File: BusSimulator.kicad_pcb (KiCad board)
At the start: 2 copper layers, 101.6 x 53.3 mm, 18 parts, among them J1 CONN_3-6318491-6, J2 CONN_3-6318491-6, U1 MPM3620, U2 MPM3620

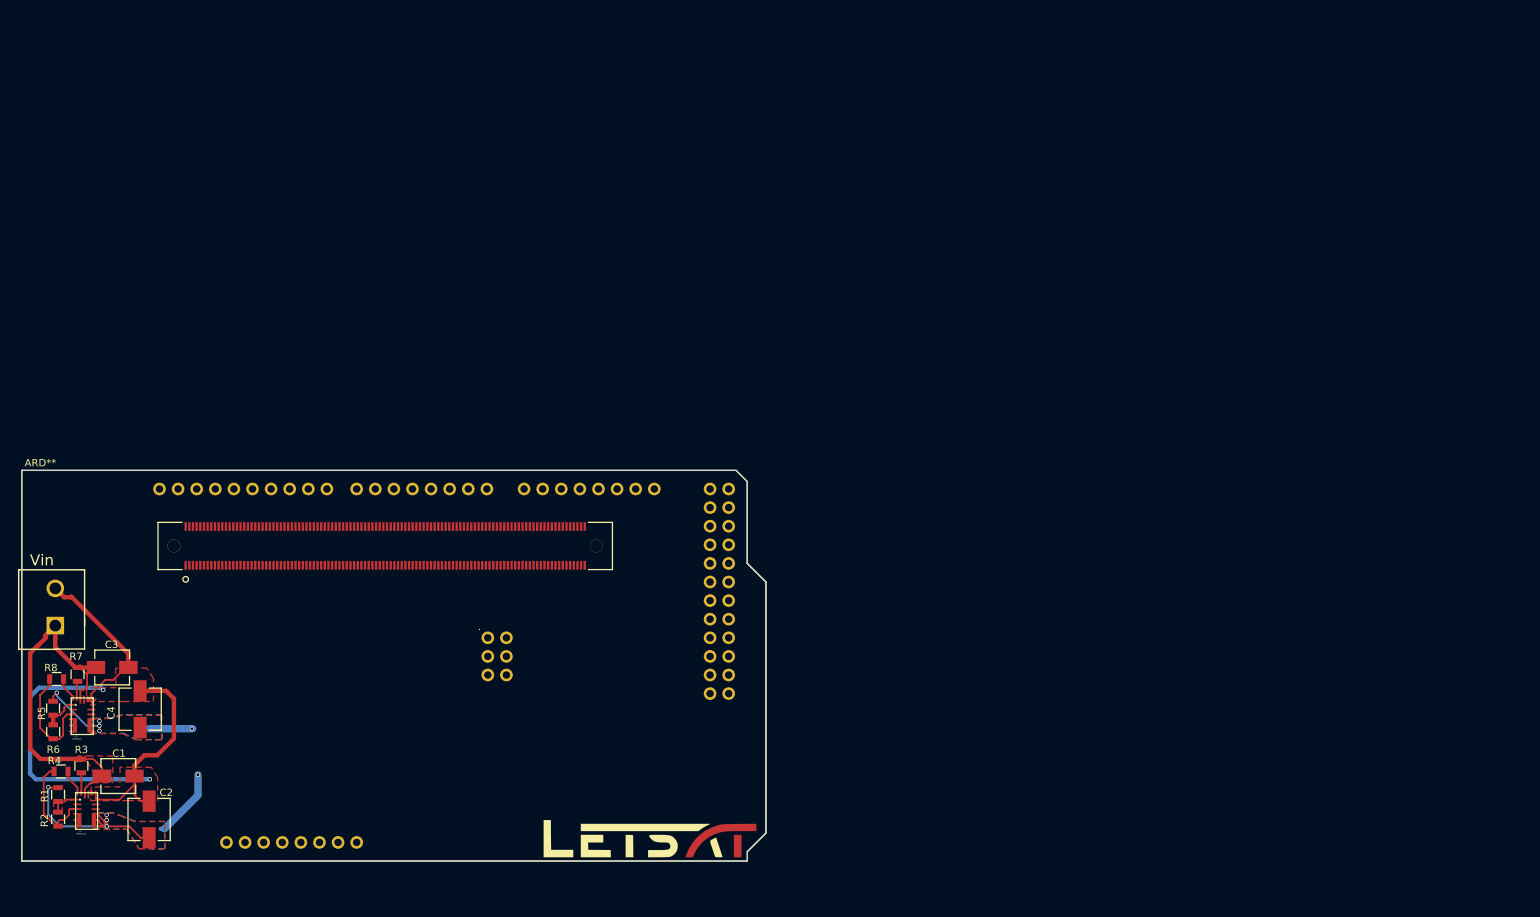
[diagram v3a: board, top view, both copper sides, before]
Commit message: pushed components on the pcb
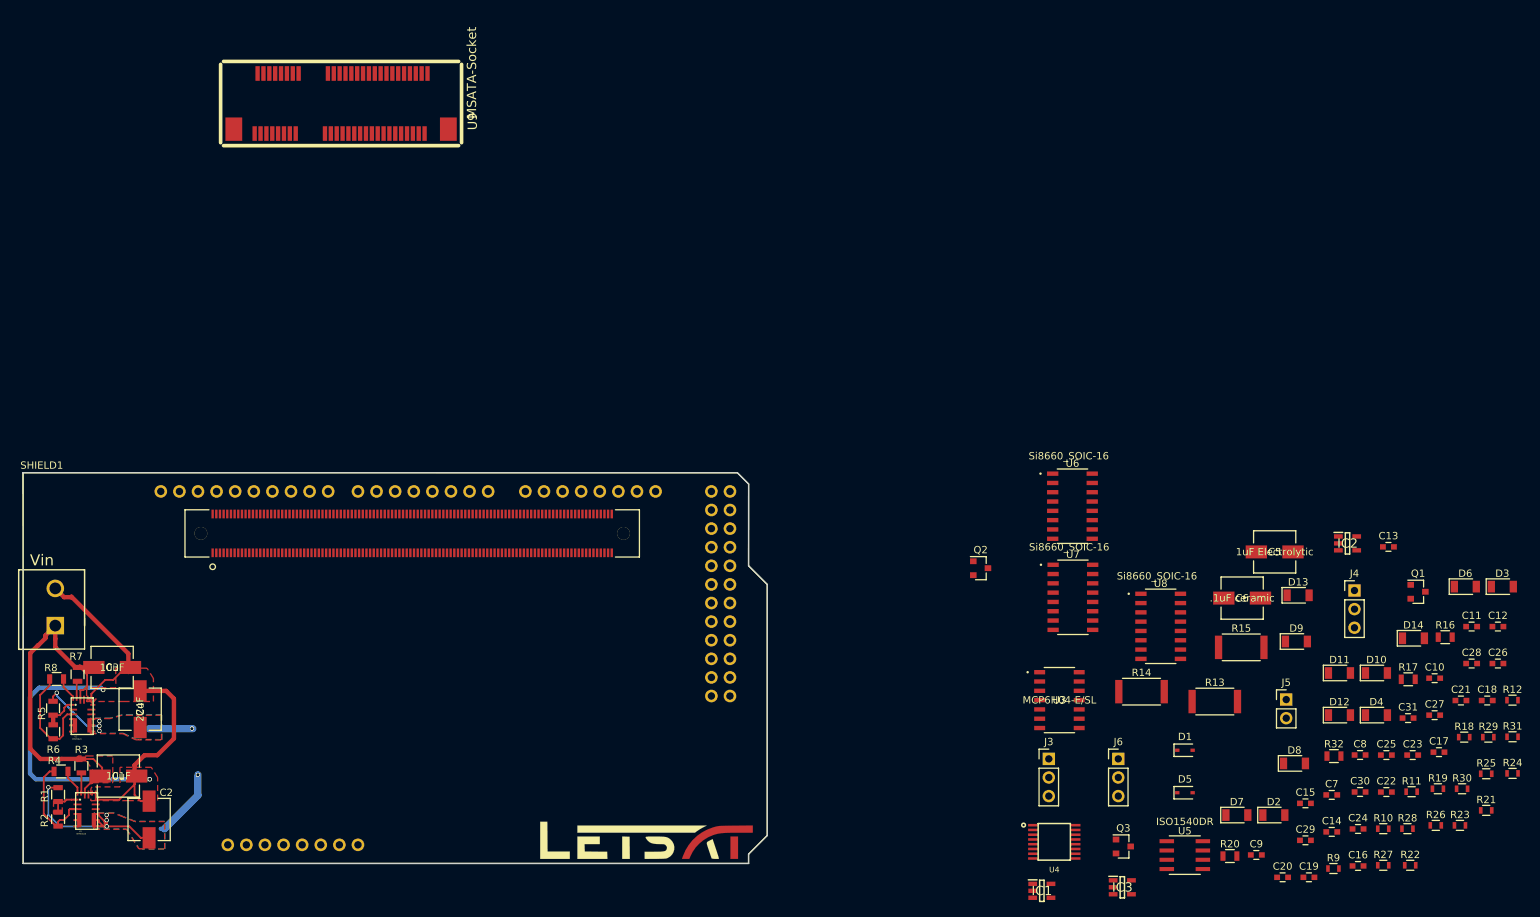
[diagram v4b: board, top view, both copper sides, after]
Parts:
- removed ARD**: Arduino_Due_Shield, BusSimulator:Arduino_Due_Shield
- added C10: .1uF, Capacitors_SMD:C_0603, F.Cu at (302.9, 116.6)
- added C11: .1uF, Capacitors_SMD:C_0603, F.Cu at (308.0, 109.6)
- added C12: .1uF, Capacitors_SMD:C_0603, F.Cu at (311.6, 109.6)
- added C13: .1uF, Capacitors_SMD:C_0603, F.Cu at (296.6, 98.7)
- added C14: .1uF, Capacitors_SMD:C_0603, F.Cu at (288.9, 137.6)
- added C15: .1uF, Capacitors_SMD:C_0603, F.Cu at (285.3, 133.7)
- added C16: .1uF, Capacitors_SMD:C_0603, F.Cu at (292.5, 142.3)
- added C17: .1uF, Capacitors_SMD:C_0603, F.Cu at (303.5, 126.7)
- added C18: .1uF, Capacitors_SMD:C_0603, F.Cu at (310.1, 119.7)
- added C19: .1uF, Capacitors_SMD:C_0603, F.Cu at (285.8, 143.8)
- added C20: .1uF, Capacitors_SMD:C_0603, F.Cu at (282.2, 143.8)
- added C21: .1uF, Capacitors_SMD:C_0603, F.Cu at (306.5, 119.7)
- added C22: .1uF, Capacitors_SMD:C_0603, F.Cu at (296.3, 132.2)
- added C23: .1uF, Capacitors_SMD:C_0603, F.Cu at (299.9, 127.1)
- added C24: .1uF, Capacitors_SMD:C_0603, F.Cu at (292.5, 137.2)
- added C25: .1uF, Capacitors_SMD:C_0603, F.Cu at (296.3, 127.1)
- added C26: .1uF, Capacitors_SMD:C_0603, F.Cu at (311.6, 114.6)
- added C27: .1uF, Capacitors_SMD:C_0603, F.Cu at (302.9, 121.7)
- added C28: .1uF, Capacitors_SMD:C_0603, F.Cu at (308.0, 114.6)
- added C29: .1uF, Capacitors_SMD:C_0603, F.Cu at (285.3, 138.8)
- added C30: .1uF, Capacitors_SMD:C_0603, F.Cu at (292.7, 132.2)
- added C31: .1uF, Capacitors_SMD:C_0603, F.Cu at (299.3, 122.1)
- added C5: 1uF Electrolytic, BusSimulator:C22, F.Cu at (281.1, 99.4)
- added C6: .1uF ceramic, BusSimulator:C22, F.Cu at (276.6, 105.7)
- added C7: .1uF, Capacitors_SMD:C_0603, F.Cu at (288.9, 132.6)
- added C8: .1uF, Capacitors_SMD:C_0603, F.Cu at (292.7, 127.1)
- added C9: .1uF, Capacitors_SMD:C_0603, F.Cu at (278.6, 140.8)
- added D1: D_Zener 9V, Diodes_SMD:D_SOD-323, F.Cu at (268.8, 126.5)
- added D10: LED, Diodes_SMD:D_1206, F.Cu at (295.0, 115.9)
- added D11: LED, Diodes_SMD:D_1206, F.Cu at (289.9, 115.9)
- added D12: LED, Diodes_SMD:D_1206, F.Cu at (289.9, 121.7)
- added D13: LED, Diodes_SMD:D_1206, F.Cu at (284.3, 105.3)
- added D14: LED, Diodes_SMD:D_1206, F.Cu at (300.0, 111.2)
- added D2: LED, Diodes_SMD:D_1206, F.Cu at (281.0, 135.3)
- added D3: LED, Diodes_SMD:D_1206, F.Cu at (312.2, 104.1)
- added D4: LED, Diodes_SMD:D_1206, F.Cu at (295.0, 121.7)
- added D5: D_Zener 9V, Diodes_SMD:D_SOD-323, F.Cu at (268.8, 132.3)
- added D6: LED, Diodes_SMD:D_1206, F.Cu at (307.1, 104.1)
- added D7: LED, Diodes_SMD:D_1206, F.Cu at (275.9, 135.3)
- added D8: LED, Diodes_SMD:D_1206, F.Cu at (283.8, 128.3)
- added D9: LED, Diodes_SMD:D_1206, F.Cu at (284.0, 111.6)
- added IC1: CS30CL, BusSimulator:SOT95P280X145-5N, F.Cu at (249.3, 145.7)
- added IC2: CS30CL, BusSimulator:SOT95P280X145-5N, F.Cu at (291.0, 98.2)
- added IC3: CS30CL, BusSimulator:SOT95P280X145-5N, F.Cu at (260.3, 145.2)
- added J3: Conn_01x03, Pin_Headers:Pin_Header_Straight_1x03_Pitch2.54mm, F.Cu at (250.2, 127.6)
- added J4: Conn_01x03, Pin_Headers:Pin_Header_Straight_1x03_Pitch2.54mm, F.Cu at (292.0, 104.7)
- added J5: Conn_01x02, Pin_Headers:Pin_Header_Straight_1x02_Pitch2.54mm, F.Cu at (282.7, 119.5)
- added J6: Conn_01x03, Pin_Headers:Pin_Header_Straight_1x03_Pitch2.54mm, F.Cu at (259.7, 127.6)
- added Q1: MOSFET_N, TO_SOT_Packages_SMD:SOT-23, F.Cu at (300.7, 104.8)
- added Q2: MOSFET_N, TO_SOT_Packages_SMD:SOT-23, F.Cu at (240.9, 101.6)
- added Q3: MOSFET_N, TO_SOT_Packages_SMD:SOT-23, F.Cu at (260.4, 139.6)
- added R10: 10k, Resistors_SMD:R_0603, F.Cu at (295.9, 137.2)
- added R11: 30k, Resistors_SMD:R_0603, F.Cu at (299.8, 132.1)
- added R12: 10k, Resistors_SMD:R_0603, F.Cu at (313.6, 119.6)
- added R13: Dummy Load, Resistors_SMD:R_2512, F.Cu at (272.9, 119.8)
- added R14: Dummy Load, Resistors_SMD:R_2512, F.Cu at (262.9, 118.5)
- added R15: Dummy Load, Resistors_SMD:R_2512, F.Cu at (276.5, 112.4)
- added R16: 25m, Resistors_SMD:R_0805, F.Cu at (304.4, 111.0)
- added R17: 25m, Resistors_SMD:R_0805, F.Cu at (299.3, 116.8)
- added R18: 1k, Resistors_SMD:R_0603, F.Cu at (307.0, 124.7)
- added R19: 330, Resistors_SMD:R_0603, F.Cu at (303.4, 131.7)
- added R20: 25m, Resistors_SMD:R_0805, F.Cu at (275.0, 140.9)
- added R21: 180, Resistors_SMD:R_0603, F.Cu at (310.0, 134.7)
- added R22: 100k, Resistors_SMD:R_0603, F.Cu at (299.6, 142.2)
- added R23: 330, Resistors_SMD:R_0603, F.Cu at (306.4, 136.7)
- added R24: 180, Resistors_SMD:R_0603, F.Cu at (313.6, 129.6)
- added R25: 1k, Resistors_SMD:R_0603, F.Cu at (310.0, 129.7)
- added R26: 330, Resistors_SMD:R_0603, F.Cu at (303.1, 136.7)
- added R27: 330, Resistors_SMD:R_0603, F.Cu at (295.9, 142.2)
- added R28: 330, Resistors_SMD:R_0603, F.Cu at (299.2, 137.2)
- added R29: 330, Resistors_SMD:R_0603, F.Cu at (310.3, 124.7)
- added R30: 330, Resistors_SMD:R_0603, F.Cu at (306.7, 131.7)
- added R31: 330, Resistors_SMD:R_0603, F.Cu at (313.6, 124.6)
- added R32: 0, Resistors_SMD:R_0805, F.Cu at (289.2, 127.3)
- added R9: 10k, Resistors_SMD:R_0603, F.Cu at (289.1, 142.6)
- added SHIELD1: ARDUINO_DUE_SHIELD, BusSimulator:Arduino_Due_Shield, F.Cu at (110.2, 141.9)
- added U3: MCP6H04-E/SL, BusSimulator:MCP6H04-E, F.Cu at (251.7, 119.6)
- added U4: ADC128D818CIMTX, BusSimulator:ADC128D818CIMTX, F.Cu at (251.0, 139.0)
- added U5: ISO1540DR, BusSimulator:ISO1540DR, F.Cu at (268.8, 140.8)
- added U6: Si8660_SOIC-16, BusSimulator:SI8660BA-B-IS1, F.Cu at (253.5, 93.1)
- added U7: Si8660_SOIC-16, BusSimulator:SI8660BA-B-IS1, F.Cu at (253.5, 105.6)
- added U8: Si8660_SOIC-16, BusSimulator:SI8660BA-B-IS1, F.Cu at (265.5, 109.5)
- added U9: MSATA-Socket, BusSimulator:msata-socket, F.Cu at (141.1, 38.2)
- C1, C3: footprint BusSimulator:EEE-1EA100WR -> BusSimulator:C22
- C4: footprint BusSimulator:EEE-1EA220WR -> BusSimulator:C22
- J2: value CONN_3-6318491-6 -> OSTTA024163
- moved J1 4.06 mm to (128.6, 94.2)
- moved G1 0.53 mm to (195.4, 139.0)
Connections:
- net +12V renamed 12v_sense
- net +3V3 renamed +3.3V
- C1 pad 1: GNDREF -> mCOM_GND
- C2 pad 1: GNDREF -> mCOM_GND
- C2 pad 2: +5V -> mCOM_5V_SBY
- C3 pad 1: GNDREF -> mCOM_GND
- C4 pad 1: GNDREF -> mCOM_GND
- J1 pad 1: (no net) -> mCOM_GND
- J1 pad 10: (no net) -> Net-(J1-Pad10)
- J1 pad 100: (no net) -> mCOM_GND
- J1 pad 101: (no net) -> Net-(J1-Pad101)
- J1 pad 102: (no net) -> Net-(J1-Pad102)
- J1 pad 103: (no net) -> Net-(J1-Pad103)
- J1 pad 104: (no net) -> mCOM_12V
- J1 pad 105: (no net) -> mCOM_12V
- J1 pad 106: (no net) -> mCOM_12V
- J1 pad 107: (no net) -> mCOM_12V
- J1 pad 108: (no net) -> mCOM_12V
- J1 pad 109: (no net) -> mCOM_12V
- J1 pad 11: (no net) -> mCOM_GND
- J1 pad 110: (no net) -> mCOM_GND
- J1 pad 111: (no net) -> mCOM_GND
- J1 pad 112: (no net) -> Net-(J1-Pad112)
- J1 pad 113: (no net) -> Net-(J1-Pad113)
- J1 pad 114: (no net) -> Net-(J1-Pad114)
- J1 pad 115: (no net) -> Net-(J1-Pad115)
- J1 pad 116: (no net) -> Net-(J1-Pad116)
- J1 pad 117: (no net) -> Net-(J1-Pad117)
- J1 pad 118: (no net) -> Net-(J1-Pad118)
- J1 pad 119: (no net) -> Net-(J1-Pad119)
- J1 pad 12: (no net) -> Net-(J1-Pad12)
- J1 pad 120: (no net) -> Net-(J1-Pad120)
- J1 pad 121: (no net) -> mCOM_GND
- J1 pad 122: (no net) -> PWRBTNn
- J1 pad 123: (no net) -> Net-(J1-Pad123)
- J1 pad 124: (no net) -> Net-(J1-Pad124)
- J1 pad 125: (no net) -> Net-(J1-Pad125)
- J1 pad 126: (no net) -> Net-(J1-Pad126)
- J1 pad 127: (no net) -> Net-(J1-Pad127)
- J1 pad 128: (no net) -> Net-(J1-Pad128)
- J1 pad 129: (no net) -> Net-(J1-Pad129)
- J1 pad 13: (no net) -> Net-(J1-Pad13)
- J1 pad 130: (no net) -> Net-(J1-Pad130)
- J1 pad 131: (no net) -> mCOM_GND
- J1 pad 132: (no net) -> Net-(J1-Pad132)
- J1 pad 133: (no net) -> Net-(J1-Pad133)
- J1 pad 134: (no net) -> PWR_OK
- J1 pad 135: (no net) -> Net-(J1-Pad135)
- J1 pad 136: (no net) -> Net-(J1-Pad136)
- J1 pad 137: (no net) -> Net-(J1-Pad137)
- J1 pad 138: (no net) -> Net-(J1-Pad138)
- J1 pad 139: (no net) -> Net-(J1-Pad139)
- J1 pad 14: (no net) -> Net-(J1-Pad14)
- J1 pad 140: (no net) -> Net-(J1-Pad140)
- J1 pad 141: (no net) -> mCOM_GND
- J1 pad 142: (no net) -> Net-(J1-Pad142)
- J1 pad 143: (no net) -> I2C_CK
- J1 pad 144: (no net) -> I2C_DAT
- J1 pad 145: (no net) -> Net-(J1-Pad145)
- J1 pad 146: (no net) -> Net-(J1-Pad146)
- J1 pad 147: (no net) -> Net-(J1-Pad147)
- J1 pad 148: (no net) -> Net-(J1-Pad148)
- J1 pad 149: (no net) -> Net-(J1-Pad149)
- J1 pad 15: (no net) -> Net-(J1-Pad15)
- J1 pad 150: (no net) -> Net-(J1-Pad150)
- J1 pad 151: (no net) -> mCOM_GND
- J1 pad 152: (no net) -> Net-(J1-Pad152)
- J1 pad 153: (no net) -> Net-(J1-Pad153)
- J1 pad 154: (no net) -> Net-(J1-Pad154)
- J1 pad 155: (no net) -> Net-(J1-Pad155)
- J1 pad 156: (no net) -> Net-(J1-Pad156)
- J1 pad 157: (no net) -> Net-(J1-Pad157)
- J1 pad 158: (no net) -> Net-(J1-Pad158)
- J1 pad 159: (no net) -> SYS_RESETn
- J1 pad 16: (no net) -> SATA0_TX+
- J1 pad 160: (no net) -> Net-(J1-Pad160)
- J1 pad 161: (no net) -> mCOM_GND
- J1 pad 162: (no net) -> Net-(J1-Pad162)
- J1 pad 163: (no net) -> Net-(J1-Pad163)
- J1 pad 164: (no net) -> GPO1
- J1 pad 165: (no net) -> Net-(J1-Pad165)
- J1 pad 166: (no net) -> Net-(J1-Pad166)
- J1 pad 167: (no net) -> GPO2
- J1 pad 168: (no net) -> Net-(J1-Pad168)
- J1 pad 169: (no net) -> Net-(J1-Pad169)
- J1 pad 17: (no net) -> SATA0_TX-
- J1 pad 170: (no net) -> mCOM_GND
- J1 pad 171: (no net) -> Net-(J1-Pad171)
- J1 pad 172: (no net) -> Net-(J1-Pad172)
- J1 pad 173: (no net) -> GPO3
- J1 pad 174: (no net) -> Net-(J1-Pad174)
- J1 pad 175: (no net) -> Net-(J1-Pad175)
- J1 pad 176: (no net) -> Net-(J1-Pad176)
- J1 pad 177: (no net) -> WAKE1n
- J1 pad 178: (no net) -> Net-(J1-Pad178)
- J1 pad 179: (no net) -> Net-(J1-Pad179)
- J1 pad 18: (no net) -> Net-(J1-Pad18)
- J1 pad 180: (no net) -> mCOM_GND
- J1 pad 181: (no net) -> Net-(J1-Pad181)
- J1 pad 182: (no net) -> Net-(J1-Pad182)
- J1 pad 183: (no net) -> Net-(J1-Pad183)
- J1 pad 184: (no net) -> Net-(J1-Pad184)
- J1 pad 185: (no net) -> Net-(J1-Pad185)
- J1 pad 186: (no net) -> Net-(J1-Pad186)
- J1 pad 187: (no net) -> Net-(J1-Pad187)
- J1 pad 188: (no net) -> Net-(J1-Pad188)
- J1 pad 189: (no net) -> Net-(J1-Pad189)
- J1 pad 19: (no net) -> SATA0_RX+
- J1 pad 190: (no net) -> mCOM_GND
- J1 pad 191: (no net) -> Net-(J1-Pad191)
- J1 pad 192: (no net) -> Net-(J1-Pad192)
- J1 pad 193: (no net) -> Net-(J1-Pad193)
- J1 pad 194: (no net) -> mCOM_5V_SBY
- J1 pad 195: (no net) -> mCOM_5V_SBY
- J1 pad 196: (no net) -> mCOM_5V_SBY
- J1 pad 197: (no net) -> mCOM_5V_SBY
- J1 pad 198: (no net) -> Net-(J1-Pad198)
- J1 pad 199: (no net) -> Net-(J1-Pad199)
- J1 pad 2: (no net) -> Net-(J1-Pad2)
- J1 pad 20: (no net) -> SATA0_RX-
- J1 pad 200: (no net) -> mCOM_GND
- J1 pad 201: (no net) -> Net-(J1-Pad201)
- J1 pad 202: (no net) -> Net-(J1-Pad202)
- J1 pad 203: (no net) -> Net-(J1-Pad203)
- J1 pad 204: (no net) -> Net-(J1-Pad204)
- J1 pad 205: (no net) -> Net-(J1-Pad205)
- J1 pad 206: (no net) -> Net-(J1-Pad206)
- J1 pad 207: (no net) -> Net-(J1-Pad207)
- J1 pad 208: (no net) -> Net-(J1-Pad208)
- J1 pad 209: (no net) -> Net-(J1-Pad209)
- J1 pad 21: (no net) -> mCOM_GND
- J1 pad 210: (no net) -> mCOM_GND
- J1 pad 211: (no net) -> Net-(J1-Pad211)
- J1 pad 212: (no net) -> Net-(J1-Pad212)
- J1 pad 213: (no net) -> SLEEPn
- J1 pad 214: (no net) -> mCOM_12V
- J1 pad 215: (no net) -> mCOM_12V
- J1 pad 216: (no net) -> mCOM_12V
- J1 pad 217: (no net) -> mCOM_12V
- J1 pad 218: (no net) -> mCOM_12V
- J1 pad 219: (no net) -> mCOM_12V
- J1 pad 22: (no net) -> Net-(J1-Pad22)
- J1 pad 220: (no net) -> mCOM_GND
- J1 pad 23: (no net) -> Net-(J1-Pad23)
- J1 pad 24: (no net) -> Net-(J1-Pad24)
- J1 pad 25: (no net) -> Net-(J1-Pad25)
- J1 pad 26: (no net) -> Net-(J1-Pad26)
- J1 pad 27: (no net) -> Net-(J1-Pad27)
- J1 pad 28: (no net) -> SATA_ACTn
- J1 pad 29: (no net) -> Net-(J1-Pad29)
- J1 pad 3: (no net) -> Net-(J1-Pad3)
- J1 pad 30: (no net) -> Net-(J1-Pad30)
- J1 pad 31: (no net) -> mCOM_GND
- J1 pad 32: (no net) -> Net-(J1-Pad32)
- J1 pad 33: (no net) -> Net-(J1-Pad33)
- J1 pad 34: (no net) -> Net-(J1-Pad34)
- J1 pad 35: (no net) -> Net-(J1-Pad35)
- J1 pad 36: (no net) -> Net-(J1-Pad36)
- J1 pad 37: (no net) -> Net-(J1-Pad37)
- J1 pad 38: (no net) -> Net-(J1-Pad38)
- J1 pad 39: (no net) -> Net-(J1-Pad39)
- J1 pad 4: (no net) -> Net-(J1-Pad4)
- J1 pad 40: (no net) -> Net-(J1-Pad40)
- J1 pad 41: (no net) -> mCOM_GND
- J1 pad 42: (no net) -> Net-(J1-Pad42)
- J1 pad 43: (no net) -> Net-(J1-Pad43)
- J1 pad 44: (no net) -> Net-(J1-Pad44)
- J1 pad 45: (no net) -> Net-(J1-Pad45)
- J1 pad 46: (no net) -> Net-(J1-Pad46)
- J1 pad 47: (no net) -> Net-(J1-Pad47)
- J1 pad 48: (no net) -> Net-(J1-Pad48)
- J1 pad 49: (no net) -> Net-(J1-Pad49)
- J1 pad 5: (no net) -> Net-(J1-Pad5)
- J1 pad 50: (no net) -> Net-(J1-Pad50)
- J1 pad 51: (no net) -> mCOM_GND
- J1 pad 52: (no net) -> Net-(J1-Pad52)
- J1 pad 53: (no net) -> Net-(J1-Pad53)
- J1 pad 54: (no net) -> GPI0
- J1 pad 55: (no net) -> Net-(J1-Pad55)
- J1 pad 56: (no net) -> Net-(J1-Pad56)
- J1 pad 57: (no net) -> mCOM_GND
- J1 pad 58: (no net) -> Net-(J1-Pad58)
- J1 pad 59: (no net) -> Net-(J1-Pad59)
- J1 pad 6: (no net) -> Net-(J1-Pad6)
- J1 pad 60: (no net) -> mCOM_GND
- J1 pad 61: (no net) -> Net-(J1-Pad61)
- J1 pad 62: (no net) -> Net-(J1-Pad62)
- J1 pad 63: (no net) -> GPI1
- J1 pad 64: (no net) -> Net-(J1-Pad64)
- J1 pad 65: (no net) -> Net-(J1-Pad65)
- J1 pad 66: (no net) -> mCOM_GND
- J1 pad 67: (no net) -> GPI2
- J1 pad 68: (no net) -> Net-(J1-Pad68)
- J1 pad 69: (no net) -> Net-(J1-Pad69)
- J1 pad 7: (no net) -> Net-(J1-Pad7)
- J1 pad 70: (no net) -> mCOM_GND
- J1 pad 71: (no net) -> Net-(J1-Pad71)
- J1 pad 72: (no net) -> Net-(J1-Pad72)
- J1 pad 73: (no net) -> Net-(J1-Pad73)
- J1 pad 74: (no net) -> Net-(J1-Pad74)
- J1 pad 75: (no net) -> Net-(J1-Pad75)
- J1 pad 76: (no net) -> Net-(J1-Pad76)
- J1 pad 77: (no net) -> Net-(J1-Pad77)
- J1 pad 78: (no net) -> Net-(J1-Pad78)
- J1 pad 79: (no net) -> Net-(J1-Pad79)
- J1 pad 8: (no net) -> Net-(J1-Pad8)
- J1 pad 80: (no net) -> mCOM_GND
- J1 pad 81: (no net) -> Net-(J1-Pad81)
- J1 pad 82: (no net) -> Net-(J1-Pad82)
- J1 pad 83: (no net) -> Net-(J1-Pad83)
- J1 pad 84: (no net) -> Net-(J1-Pad84)
- J1 pad 85: (no net) -> GPI3
- J1 pad 86: (no net) -> Net-(J1-Pad86)
- J1 pad 87: (no net) -> Net-(J1-Pad87)
- J1 pad 88: (no net) -> Net-(J1-Pad88)
- J1 pad 89: (no net) -> Net-(J1-Pad89)
- J1 pad 9: (no net) -> Net-(J1-Pad9)
- J1 pad 90: (no net) -> mCOM_GND
- J1 pad 91: (no net) -> Net-(J1-Pad91)
- J1 pad 92: (no net) -> Net-(J1-Pad92)
- J1 pad 93: (no net) -> GPO0
- J1 pad 94: (no net) -> Net-(J1-Pad94)
- J1 pad 95: (no net) -> Net-(J1-Pad95)
- J1 pad 96: (no net) -> Net-(J1-Pad96)
- J1 pad 97: (no net) -> Net-(J1-Pad97)
- J1 pad 98: (no net) -> SER0_TX
- J1 pad 99: (no net) -> SER0_RX
- J2 pad 2: GNDREF -> mCOM_GND
- R1 pad 1: +5V -> mCOM_5V_SBY
- U1 pad 12: GNDREF -> mCOM_GND
- U1 pad 13: GNDREF -> mCOM_GND
- U1 pad 14: GNDREF -> mCOM_GND
- U1 pad 7: +5V -> mCOM_5V_SBY
- U1 pad 8: +5V -> mCOM_5V_SBY
- U1 pad 9: +5V -> mCOM_5V_SBY
- U2 pad 12: GNDREF -> mCOM_GND
- U2 pad 13: GNDREF -> mCOM_GND
- U2 pad 14: GNDREF -> mCOM_GND
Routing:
- net mCOM_GND: track 0.00 -> 58.9 mm
- net GNDREF: track 58.9 -> 0.00 mm
- net mCOM_5V_SBY: track 0.00 -> 26.9 mm, vias 0 -> 4
- net +5V: track 26.9 -> 0.00 mm, vias 4 -> 0
- added copper zone on B.Cu, net +3V3
- added copper zone on F.Cu, net +3V3
- removed copper zone on B.Cu, net +3.3V
- removed copper zone on F.Cu, net +3.3V
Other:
- board size 101.6 x 53.3 mm -> 101.6 x 53.4 mm

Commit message: started pcb
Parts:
- C15, C22, C6, R11, R12, U4, U6, U7, U8: moved to B.Cu
- moved R12 197.0 mm to (117.1, 105.2), turned to 90 degrees
- moved C22 186.7 mm to (112.6, 99.4), turned to 135 degrees
- moved R22 186.5 mm to (119.5, 93.6), turned to 180 degrees
- moved R11 184.1 mm to (117.1, 109.0), turned to 90 degrees
- moved J5 168.9 mm to (115.6, 95.0), turned to 315 degrees
- moved C15 164.3 mm to (123.4, 105.4), turned to 90 degrees
- moved R10 164.1 mm to (131.8, 133.6), turned to 270 degrees
- moved R9 157.4 mm to (131.9, 136.3), turned to 90 degrees
- moved C5 147.4 mm to (133.8, 105.6), turned to 180 degrees
- moved U5 145.3 mm to (130.3, 97.0), turned to 90 degrees
- moved IC2 144.6 mm to (147.5, 115.1)
- moved C6 142.8 mm to (133.8, 105.8), turned to 270 degrees
- moved U3 129.2 mm to (123.3, 104.5), turned to 180 degrees
- moved U4 125.2 mm to (130.3, 105.5), turned to 270 degrees
- moved U8 108.5 mm to (157.7, 97.1), turned to 270 degrees
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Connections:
- SHIELD1 pad SCL1: Net-(SHIELD1-PadSCL1) -> DUE_SCL
- SHIELD1 pad SDA1: Net-(SHIELD1-PadSDA1) -> DUE_SDA
- U3 pad 12: Net-(U3-Pad12) -> Temp
- U3 pad 13: Net-(U3-Pad13) -> VoutD
- U4 pad 9: Temp -> Net-(U4-Pad9)
- U7 pad 8: mCOM_GND -> GND
- U7 pad 9: GND -> mCOM_GND
- U8 pad 8: mCOM_GND -> GND
- U8 pad 9: GND -> mCOM_GND
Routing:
- net FC3V3: track 0.00 -> 191.9 mm, vias 0 -> 1
- net mCOM_5V_SBY: track 26.9 -> 126.7 mm, vias 4 -> 11
- net mCOM_GND: track 58.9 -> 131.9 mm, vias 0 -> 5
- net +3.3V: track 10.7 -> 50.6 mm, vias 4 -> 7
- net +2.5V: track 0.00 -> 37.5 mm, vias 0 -> 4
- net GPI0: track 0.00 -> 29.6 mm, vias 0 -> 1
- net ISOSERO_Rx: track 0.00 -> 29.1 mm, vias 0 -> 1
- net GND: track 0.00 -> 28.5 mm, vias 0 -> 1
- net Temp: track 0.00 -> 22.1 mm
- net GPI2: track 0.00 -> 21.6 mm, vias 0 -> 1
- net VOutC: track 0.00 -> 21.3 mm, vias 0 -> 1
- net (no net): track 53.7 -> 34.5 mm, vias 4 -> 2
- net GPI1: track 0.00 -> 19.0 mm, vias 0 -> 1
- net VoutB: track 0.00 -> 16.2 mm, vias 0 -> 2
- net ISO_LOAD_1: track 0.00 -> 16.0 mm, vias 0 -> 1
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- added copper zone on B.Cu, net +3.3V
- added copper zone on B.Cu, net mCOM_GND
- added copper zone on F.Cu, net mCOM_GND
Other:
- outline, holes or cut-outs redrawn
- net class Default: trace_width 0.6 -> 0.2
